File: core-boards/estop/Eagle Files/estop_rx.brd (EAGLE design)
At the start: 76.2 x 50.8 mm, 34 parts, among them J1 RFM95W-3072, J2 B2PS-VH(LF)(SN), J3 B2PS-VH(LF)(SN), J4 2-PIN_2MM-V, J5 6-PIN_2MM-V, U1 R-78E5.0-1.0CONV_R-78E5.0-1.0, U2 MCP2551T-E/SN, U4 ATMEGA328P-AUR

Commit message: things should be done tm
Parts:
- added U6: D5V0L1B2WS-7, IGVC-Discrete:SOD323
- C1, C5: device rcl:C0603 -> rcl:C0805
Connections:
- net +12V: now also U6.1
- net GND: now also U6.2
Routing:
- net GND: track 46.4 -> 48.3 mm, vias 21 -> 22
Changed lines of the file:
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@@
 <layer number="24" name="bOrigins" color="15" fill="1" visible="yes" active="yes"/>
 <layer number="25" name="tNames" color="7" fill="1" visible="yes" active="yes"/>
-<layer number="26" name="bNames" color="7" fill="1" visible="yes" active="yes"/>
+<layer number="26" name="bNames" color="7" fill="1" visible="no" active="yes"/>
 <layer number="27" name="tValues" color="7" fill="1" visible="no" active="yes"/>
 <layer number="28" name="bValues" color="7" fill="1" visible="no" active="yes"/>
@@
 <attribute name="VALUE" x="76.223" y="13.233" size="1.27" layer="27" rot="R90" align="top-left"/>
 </element>
-<element name="C1" library="rcl" library_urn="urn:adsk.eagle:library:334" package="C0603" package3d_urn="urn:adsk.eagle:package:23616/2" value="10uF" x="65.541" y="9.868" smashed="yes" rot="R90">
+<element name="C1" library="rcl" library_urn="urn:adsk.eagle:library:334" package="C0805" package3d_urn="urn:adsk.eagle:package:23617/2" value="10uF" x="65.541" y="9.868" smashed="yes" rot="R90">
 <attribute name="NAME" x="64.906" y="9.233" size="0.5" layer="25" rot="R90"/>
-<attribute name="POPULARITY" value="37" x="65.541" y="9.868" size="1.778" layer="27" rot="R90" display="off"/>
+<attribute name="POPULARITY" value="63" x="65.541" y="9.868" size="1.778" layer="27" rot="R90" display="off"/>
 <attribute name="SPICEPREFIX" value="C" x="65.541" y="9.868" size="1.778" layer="27" rot="R90" display="off"/>
 <attribute name="VALUE" x="67.446" y="9.233" size="1.27" layer="27" rot="R90"/>
@@
 <attribute name="VALUE" x="38.595" y="39.585" size="1.27" layer="27"/>
 </element>
-<element name="C5" library="rcl" library_urn="urn:adsk.eagle:library:334" package="C0603" package3d_urn="urn:adsk.eagle:package:23616/2" value="10uF" x="65" y="20" smashed="yes" rot="R90">
+<element name="C5" library="rcl" library_urn="urn:adsk.eagle:library:334" package="C0805" package3d_urn="urn:adsk.eagle:package:23617/2" value="10uF" x="65" y="20" smashed="yes" rot="R90">
 <attribute name="NAME" x="64.365" y="19.365" size="0.5" layer="25" rot="R90"/>
-<attribute name="POPULARITY" value="37" x="65" y="20" size="1.778" layer="27" rot="R90" display="off"/>
+<attribute name="POPULARITY" value="63" x="65" y="20" size="1.778" layer="27" rot="R90" display="off"/>
 <attribute name="SPICEPREFIX" value="C" x="65" y="20" size="1.778" layer="27" rot="R90" display="off"/>
 <attribute name="VALUE" x="66.905" y="19.365" size="1.27" layer="27" rot="R90"/>
@@
 <attribute name="SPICEPREFIX" value="R" x="31.4" y="31.1" size="1.778" layer="27" rot="R90" display="off"/>
 <attribute name="VALUE" x="33.305" y="30.465" size="1.27" layer="27" rot="R90"/>
+</element>
+<element name="U6" library="IGVC-Discrete" package="SOD323" value="D5V0L1B2WS-7" x="71.3" y="11.6" smashed="yes">
+<attribute name="BUILT_BY" value="EMA_UL_Team" x="71.3" y="11.6" size="1.778" layer="27" display="off"/>
+<attribute name="MANUFACTURER_PART_NUMBER" value="D5V0L1B2WS-7" x="71.3" y="11.6" size="1.778" layer="27" display="off"/>
+<attribute name="NAME" x="68.0234" y="10.965" size="0.5" layer="25" ratio="6" rot="SR0"/>
+<attribute name="VENDOR" value="Diodes Inc" x="71.3" y="11.6" size="1.778" layer="27" display="off"/>
 </element>
 </elements>
@@
 <vertex x="0.18" y="0.17"/>
 </polygon>
-<wire x1="65.541" y1="10.718" x2="65.541" y2="11" width="0.4064" layer="1"/>
+<wire x1="65.541" y1="10.818" x2="65.541" y2="11" width="0.4064" layer="1"/>
 <wire x1="65.541" y1="11" x2="67" y2="11" width="0.4064" layer="1"/>
 <via x="67" y="11" extent="1-16" drill="0.35"/>
@@
 <wire x1="58.999" y1="46.999" x2="59" y2="47" width="0.4064" layer="1"/>
 <via x="59" y="47" extent="1-16" drill="0.35"/>
-<wire x1="65" y1="20.85" x2="64.85" y2="21" width="0.4064" layer="1"/>
-<wire x1="64.85" y1="21" x2="63" y2="21" width="0.4064" layer="1"/>
-<via x="63" y="21" extent="1-16" drill="0.35"/>
+<contactref element="U6" pad="2"/>
+<wire x1="72.45" y1="11.6" x2="73.6" y2="11.6" width="0.4064" layer="1"/>
+<wire x1="73.6" y1="11.6" x2="74" y2="12" width="0.4064" layer="1"/>
+<via x="74" y="12" extent="1-16" drill="0.35"/>
+<wire x1="65" y1="20.95" x2="63.95" y2="20.95" width="0.4064" layer="1"/>
+<wire x1="63.95" y1="20.95" x2="63" y2="20" width="0.4064" layer="1"/>
+<via x="63" y="20" extent="1-16" drill="0.35"/>
 </signal>
 <signal name="MISO">
@@
 <wire x1="69.42706875" y1="38.5036" x2="70.35293125" y2="38.5036" width="0.254" layer="1"/>
 <wire x1="71.47053125" y1="37.386" x2="72.43" y2="37.386" width="0.254" layer="1"/>
-<wire x1="70.35293125" y1="38.5036" x2="71.47053125" y2="37.386" width="0.254" layer="1"/>
+<wire x1="70.35293125" y1="38.5036" x2="71.428265625" y2="37.428265625" width="0.254" layer="1"/>
+<wire x1="71.428265625" y1="37.428265625" x2="71.47053125" y2="37.386" width="0.254" layer="1"/>
 <wire x1="68" y1="37.07653125" x2="69.42706875" y2="38.5036" width="0.254" layer="1"/>
 <wire x1="68" y1="31.5747375" x2="68" y2="37.07653125" width="0.254" layer="1"/>
@@
 <contactref element="D14" pad="C"/>
 <contactref element="U$1" pad="P$5"/>
-<wire x1="47.246" y1="2.723" x2="38.2977375" y2="2.723" width="0.254" layer="1"/>
-<wire x1="38.2977375" y1="2.723" x2="36.7177375" y2="1.143" width="0.254" layer="1"/>
-<wire x1="36.7177375" y1="1.143" x2="30.857" y2="1.143" width="0.254" layer="1"/>
 <contactref element="J5" pad="5"/>
 <wire x1="19.637" y1="11.949" x2="19.637" y2="4.787" width="0.254" layer="1"/>
 <wire x1="19.637" y1="4.787" x2="18.04" y2="3.19" width="0.254" layer="1"/>
 <wire x1="20.051" y1="11.949" x2="19.637" y2="11.949" width="0.254" layer="1"/>
-<wire x1="30.857" y1="1.143" x2="20.051" y2="11.949" width="0.254" layer="1"/>
+<wire x1="20.051" y1="11.949" x2="30.857" y2="1.143" width="0.254" layer="1"/>
+<wire x1="45.666" y1="1.143" x2="47.246" y2="2.723" width="0.254" layer="1"/>
+<wire x1="30.857" y1="1.143" x2="45.666" y2="1.143" width="0.254" layer="1"/>
 </signal>
 <signal name="+24V">
@@
 <vertex x="64" y="0.19"/>
 </polygon>
+<contactref element="U6" pad="1"/>
 </signal>
 <signal name="CAN_P">

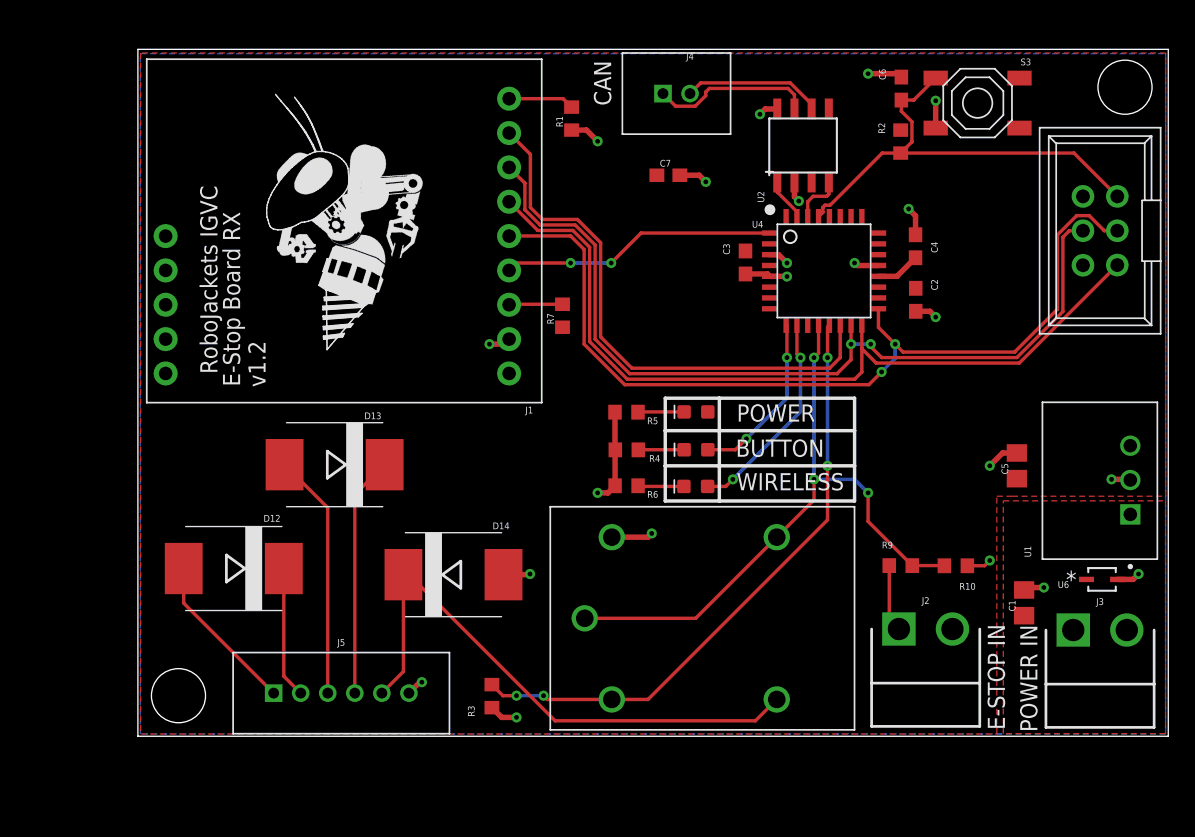
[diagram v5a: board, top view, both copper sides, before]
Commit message: Fixed estop RX
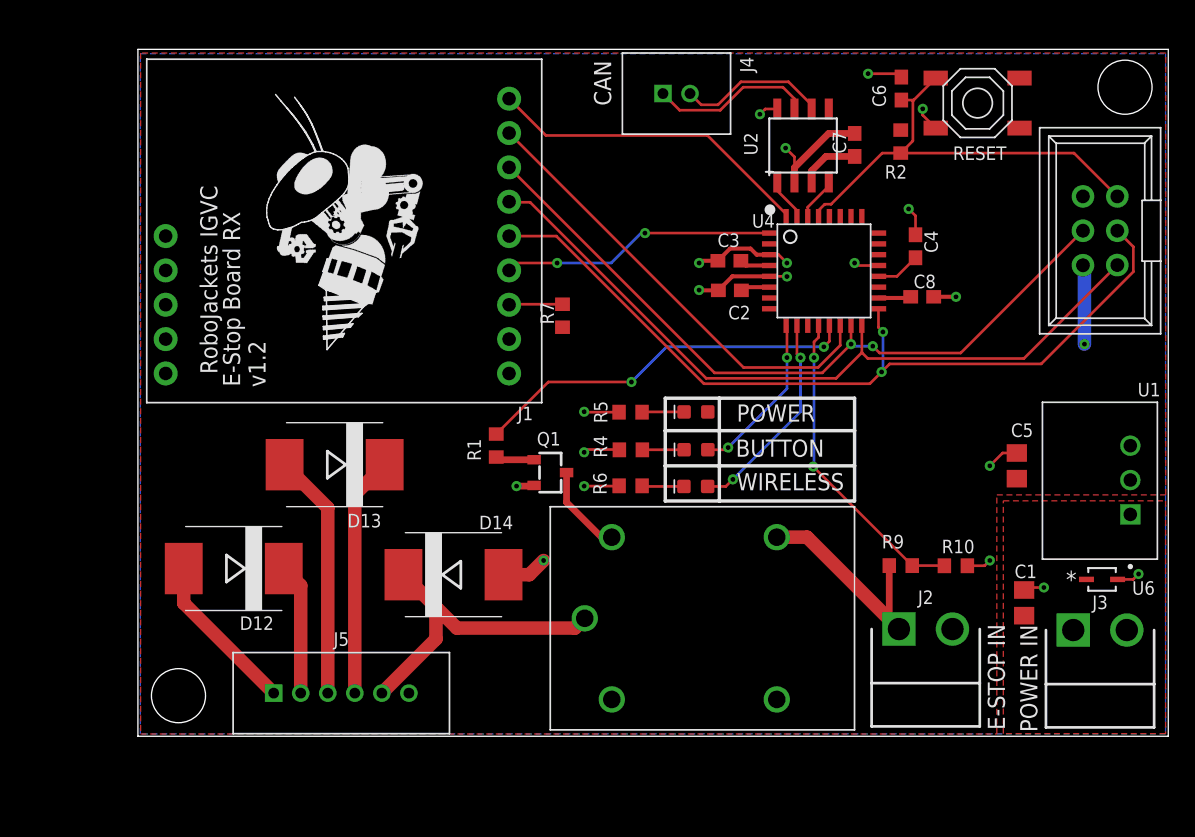
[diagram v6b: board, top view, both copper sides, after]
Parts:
- removed R3: 10k, resistor:R0603
- added C8: 0.1uF, rcl:C0603
- added Q1: BJT-NPN_, RoboJackets-Discrete:SOT-23-3
- R1: value 10k -> 1k
- moved R1 24.8 mm to (26.5, 21.5), turned to 270 degrees
- moved C7 14.0 mm to (53.0, 43.7), turned to 90 degrees
- moved C2 13.8 mm to (43.8, 33.0), turned to 180 degrees
- moved C3 1.20 mm to (43.7, 35.2), turned to 180 degrees
- moved R5 0.30 mm to (36.4, 24.0)
- moved R6 0.30 mm to (36.4, 18.5)
- moved R4 0.30 mm to (36.5, 21.2)
- renumbered S3 to RESET
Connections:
- removed net EN: U4.11
- removed net IN: R10.1, R9.2, U$1.P$2, U$1.P$4, U4.12
- removed net OUT: R3.2, U$1.P$3, U4.13
- new net ESTOP_IN: J2.1, R9.1, U$1.P$2
- new net ESTOP_MC_IN: R10.1, R9.2, U4.12
- new net RADIO_RST: J1.9, U4.32
- new net RELAY_CTRL: R1.1, U4.13
- net +5V: now also C8.1, U$1.P$3
- net GND: now also C8.2, Q1.2; no longer R1.1, R3.1, U$1.P$1
- net N$1: now also Q1.3, U$1.P$1; no longer J2.1, R9.1
- net N$5: now also Q1.1; no longer J1.9
- net SOLENOID_TRIG: now also U$1.P$4; no longer U$1.P$5
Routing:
- net IN: track 47.2 -> 0.00 mm, vias 3 -> 0
- net OUT: track 45.2 -> 0.00 mm, vias 4 -> 0
- net RELAY_CTRL: track 0.00 -> 28.7 mm, vias 0 -> 2
- net RADIO_RST: track 0.00 -> 24.2 mm
- net ESTOP_MC_IN: track 0.00 -> 23.4 mm, vias 0 -> 2
- net SOLENOID_TRIG: track 42.2 -> 23.4 mm
- net +5V: track 0.00 -> 17.2 mm, vias 0 -> 1
- net ESTOP_IN: track 0.00 -> 16.8 mm
- net MOSI: track 64.6 -> 55.0 mm
- net GND: track 48.3 -> 55.3 mm, vias 22 -> 20
- net CE: track 40.8 -> 33.8 mm
- net MISO: track 61.6 -> 56.3 mm
- net SCK: track 66.7 -> 62.5 mm
- net N$5: track 4.88 -> 2.88 mm
- net N$1: track 4.99 -> 6.61 mm
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
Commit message: Fixed estop-tx
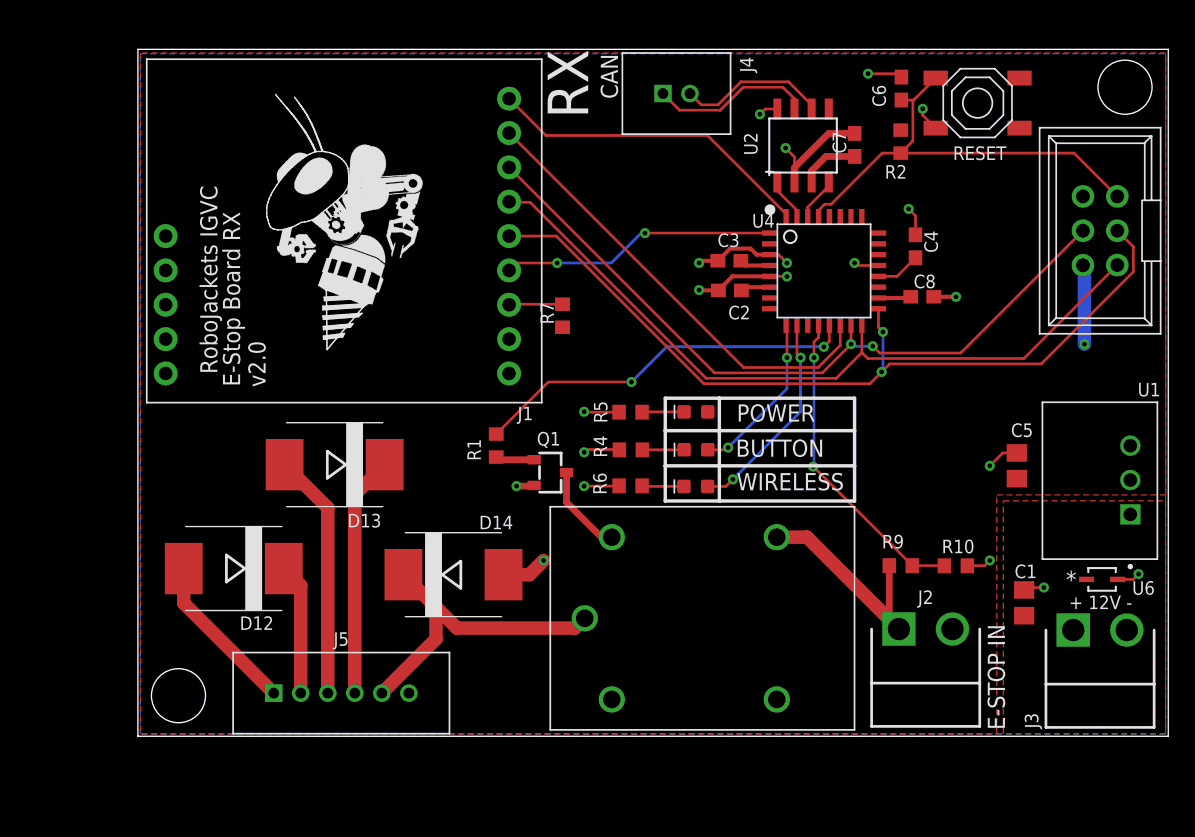
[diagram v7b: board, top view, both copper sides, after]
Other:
- board text added: "+ 12V -"
- board text added: "RX"
- board text added: "v2.0"
- board text removed: "POWER IN"
- board text removed: "v1.2"
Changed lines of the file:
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@@
 <text x="44.21" y="20.67" size="1.27" layer="21" font="vector">BUTTON</text>
 <text x="44.28" y="18.19" size="1.27" layer="21" font="vector">WIRELESS</text>
-<text x="35" y="46.63" size="1.27" layer="21" rot="R90">CAN</text>
-<text x="66.52" y="0.31" size="1.27" layer="21" rot="R90">POWER IN</text>
-<text x="64.12" y="0.47" size="1.27" layer="21" rot="R90">E-STOP IN</text>
+<text x="35.5" y="47.13" size="1.27" layer="21" font="vector" rot="R90">CAN</text>
+<text x="64.12" y="0.47" size="1.27" layer="21" font="vector" rot="R90">E-STOP IN</text>
 <text x="4.61" y="40.73" size="1.27" layer="21" font="vector" rot="R270">RoboJackets IGVC</text>
 <text x="7.56" y="25.87" size="1.27" layer="21" font="vector" rot="R90">E-Stop Board RX</text>
-<text x="9.44" y="25.82" size="1.27" layer="21" font="vector" rot="R90">v1.2</text>
+<text x="9.44" y="25.82" size="1.27" layer="21" font="vector" rot="R90">v2.0</text>
 <wire x1="39" y1="22.6" x2="39" y2="20" width="0.254" layer="21"/>
 <wire x1="39" y1="20" x2="39" y2="17.4" width="0.254" layer="21"/>
@@
 <wire x1="53" y1="20" x2="39" y2="20" width="0.254" layer="21"/>
 <wire x1="43" y1="25" x2="43" y2="17.4" width="0.254" layer="21"/>
+<text x="71.2" y="9.4" size="1" layer="21" font="vector" align="bottom-center">+ 12V -</text>
+<text x="30.3" y="45.7" size="3" layer="21" font="vector" rot="R90" align="top-left">RX</text>
 </plain>
 <attributes>
@@
 <attribute name="DIGIKEY" value="455-1648-ND" x="71.153" y="7.856" size="1.778" layer="27" display="off"/>
 <attribute name="MPN" value="B2PS-VH(LF)(SN)" x="71.153" y="7.856" size="1.778" layer="27" display="off"/>
-<attribute name="NAME" x="71.153" y="9.406" size="1" layer="25" font="vector" align="bottom-center"/>
+<attribute name="NAME" x="66.594" y="1.153" size="1" layer="25" font="vector" rot="R90" align="bottom-center"/>
 </element>
 <element name="J2" library="RoboJackets-Connectors" package="B2PS-CENTERED" value="B2PS-VH(LF)(SN)" x="58.26" y="7.93" smashed="yes">

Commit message: estop rx CAN controller added
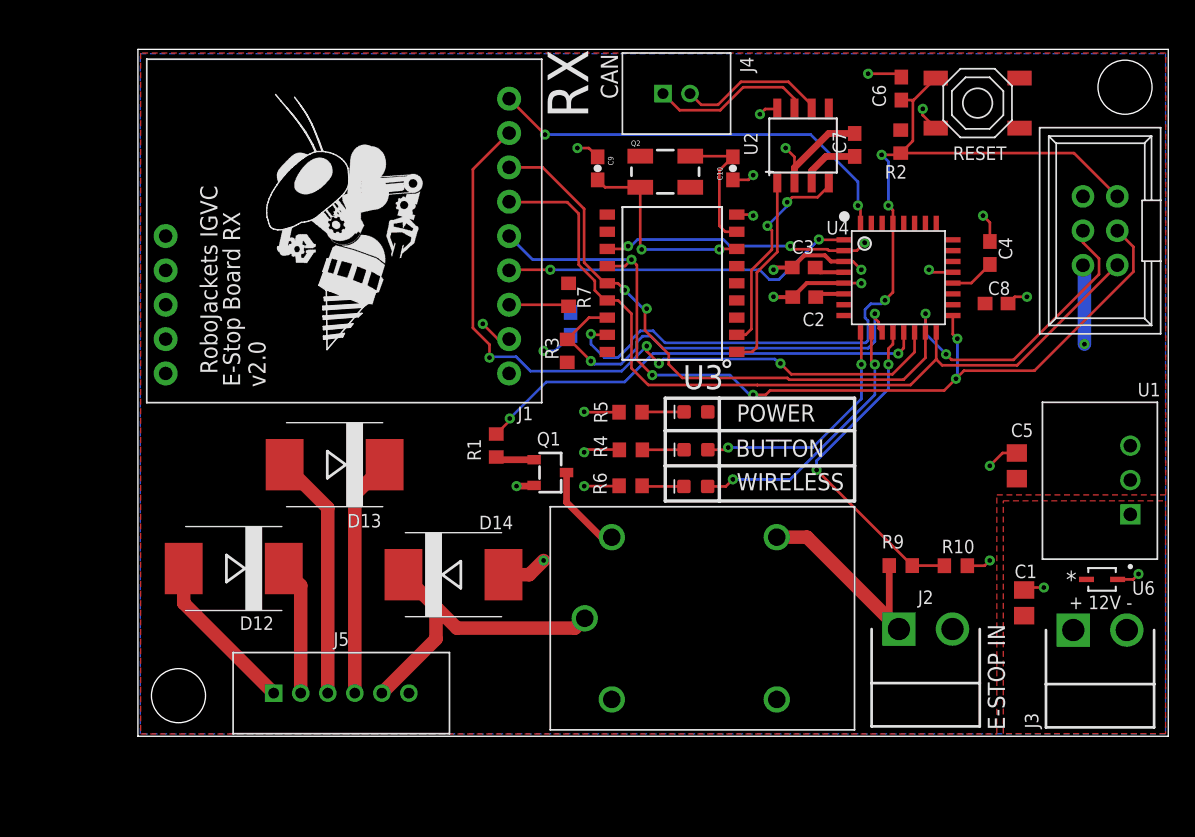
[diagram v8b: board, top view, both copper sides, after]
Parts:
- added C10, C9: 22pF, SparkFun-Capacitors:0603-CAP
- added C11: 0.1uF, SparkFun-Capacitors:0603-CAP
- added Q2: 16MHz, SparkFun-FreqCtrl:CRYSTAL-SMD-5X3
- added R3: 10k, resistor:R0603
- added U3: MCP2515, SparkFun-DigitalIC:SO-18W
- moved C2 5.52 mm to (49.3, 32.5)
- moved C3 5.52 mm to (49.2, 34.7)
- moved C4 5.52 mm to (63.0, 35.7)
- moved C8 5.52 mm to (63.5, 32.0)
- moved U4 5.52 mm to (56.2, 34.1)
- moved R7 1.61 mm to (31.9, 32.6), turned to 270 degrees
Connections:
- removed net CAN_RX: U2.4, U4.30
- removed net CAN_TX: U2.1, U4.31
- new net CAN_CS: R3.2, U3.16, U4.11
- new net CAN_INT: U3.12, U4.2
- new net CAN_RXD: U2.4, U3.2
- new net CAN_TXD: U2.1, U3.1
- new net N$17: C10.2, Q2.3, U3.8
- new net N$18: C9.2, Q2.1, U3.7
- net !RESET: now also U3.17
- net +5V: now also C11.2, R3.1, U3.18
- net GND: now also C10.1, C11.1, C9.1, U3.9
- net MISO: now also U3.15
- net MOSI: now also U3.14
- net SCK: now also U3.13
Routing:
- net !RESET: track 33.2 -> 66.2 mm, vias 0 -> 4
- net CAN_CS: track 0.00 -> 32.5 mm, vias 0 -> 2
- net CE: track 33.8 -> 54.4 mm, vias 0 -> 4
- net CAN_INT: track 0.00 -> 19.9 mm, vias 0 -> 3
- net CAN_RXD: track 0.00 -> 15.9 mm, vias 0 -> 2
- net N$18: track 0.00 -> 15.1 mm, vias 0 -> 2
- net CAN_TXD: track 0.00 -> 14.5 mm
- net MOSI: track 55.0 -> 66.7 mm, vias 2 -> 4
- net N$17: track 0.00 -> 10.2 mm
- net RADIO_RST: track 24.2 -> 31.5 mm, vias 0 -> 2
- net GND: track 55.3 -> 62.3 mm, vias 20 -> 24
- net SCK: track 62.5 -> 69.3 mm, vias 2 -> 5
- net IRQ: track 20.4 -> 26.4 mm
- net BUTTON_LED: track 12.4 -> 17.9 mm
- net MISO: track 56.3 -> 61.7 mm
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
